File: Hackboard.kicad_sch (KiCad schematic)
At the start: 66 parts, among them J1 Conn_01x31_Socket, J2 Micro_SD_Card, J3 Conn_01x31_Socket, J5 Conn_02x02_Counter_Clockwise, J6 USB_C_Receptacle_USB2.0_16P, J7 Barrel_Jack_Switch, Q1 NMOS, Q2 NMOS, Q3 NMOS, SW1 SW_DPST, U1 NCP164CSN330T1G, U2 AP63205WU, U3 STM32L476RGT6, U4 74LVC4245APW, U5 74LVC4245APW, U6 74LVC4245APW, U7 USBLC6-2SC6, U8 74LVC4245APW, U9 74LVC4245APW

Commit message: Route power
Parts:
- added R16: 1M, symbol Device:R
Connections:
- net GND: now also R16.2; no longer J6.S1 (SHIELD)
- new net: J6.S1 (SHIELD), R16.1
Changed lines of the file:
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@@
 	)
 	(junction
+		(at 229.87 162.56)
+		(diameter 0)
+		(color 0 0 0 0)
+	)
+	(junction
 		(at 246.38 106.68)
 		(diameter 0)
@@
 	)
 	(junction
-		(at 229.87 162.56)
-		(diameter 0)
-		(color 0 0 0 0)
-	)
-	(junction
 		(at 62.23 19.05)
 		(diameter 0)
@@
 		)
 	)
-	(wire
-		(pts
-			(xy 222.25 162.56) (xy 229.87 162.56)
-		)
-		(stroke
-			(width 0)
-			(type default)
-		)
-	)
 	(polyline
 		(pts
@@
 					(unit 1)
 				)
+			)
+		)
+	)
+	(symbol
+		(lib_id "Device:R")
+		(at 226.06 162.56 90)
+		(unit 1)
+		(exclude_from_sim no)
+		(in_bom yes)
+		(on_board yes)
+		(dnp no)
+		(property "Reference" "R16"
+			(at 226.06 160.528 90)
+			(effects
+				(font
+					(size 1.27 1.27)
+				)
+			)
+		)
+		(property "Value" "1M"
+			(at 226.06 164.846 90)
+			(effects
+				(font
+					(size 1.27 1.27)
+				)
+			)
+		)
+		(property "Footprint" ""
+			(at 226.06 164.338 90)
+			(effects
+				(font
+					(size 1.27 1.27)
+				)
+				(hide yes)
+			)
+		)
+		(property "Datasheet" "~"
+			(at 226.06 162.56 0)
+			(effects
+				(font
+					(size 1.27 1.27)
+				)
+				(hide yes)
+			)
+		)
+		(property "Description" "Resistor"
+			(at 226.06 162.56 0)
+			(effects
+				(font
+					(size 1.27 1.27)
+				)
+				(hide yes)
+			)
+		)
+		(pin "2"
+		)
+		(pin "1"
+		)
+		(instances
+			(project "Hackboard"
+				(path "/478098fb-f4b2-4694-bef3-d53baad1e8cf"
+					(reference "R16")
+					(unit 1)
+				)

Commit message: Change USB C footprint, fix DRC errors, adjust silkscreen
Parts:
- J6: footprint Connector_USB:USB_C_Receptacle_GCT_USB4105-xx-A_16P_TopMnt_Horizontal -> Connector_USB:USB_C_Receptacle_Molex_216990
- R16: footprint (none) -> Resistor_SMD:R_0603_1608Metric
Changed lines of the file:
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@@
 			)
 		)
-		(property "Footprint" "Connector_USB:USB_C_Receptacle_GCT_USB4105-xx-A_16P_TopMnt_Horizontal"
+		(property "Footprint" "Connector_USB:USB_C_Receptacle_Molex_216990"
 			(at 233.68 139.7 0)
 			(effects
@@
 			)
 		)
-		(property "Footprint" ""
+		(property "Footprint" "Resistor_SMD:R_0603_1608Metric"
 			(at 226.06 164.338 90)
 			(effects

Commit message: Finish PCB
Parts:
- removed SW1: SW_DPST, Button_Switch_SMD:SW_SPST_PTS645, symbol Switch:SW_DPST_x2
- added R17, R18, R19, R20: 50k, Resistor_SMD:R_0603_1608Metric, symbol Device:R
- added SW1: SW_SPST, Button_Switch_SMD:SW_SPST_PTS645, symbol Switch:SW_SPST
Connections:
- net +3V3: now also R17.1, R18.1, R19.1, R20.1
- net GND: now also SW1.1 (A)
- net PWM_PIN2: now also U6.14 (B5); no longer JP2.1 (A)
- net PWM_PIN2_O: now also JP2.2 (B); no longer U6.8 (A5)
- net RESET: now also SW1.2 (B)
- net SD_CS_PWM_26: now also R20.2
- net SD_MISO_PWM_28: now also R17.2
- net SD_MOSI_GPIO_PIN4: now also R19.2
- net SD_SCK_DAC_A8: now also R18.2
- new net: JP2.1 (A), U6.8 (A5)
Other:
- moved on the sheet: J2, J5, Q2, Q3, R10, R11, R14, R15, U4, U5, U6, U8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

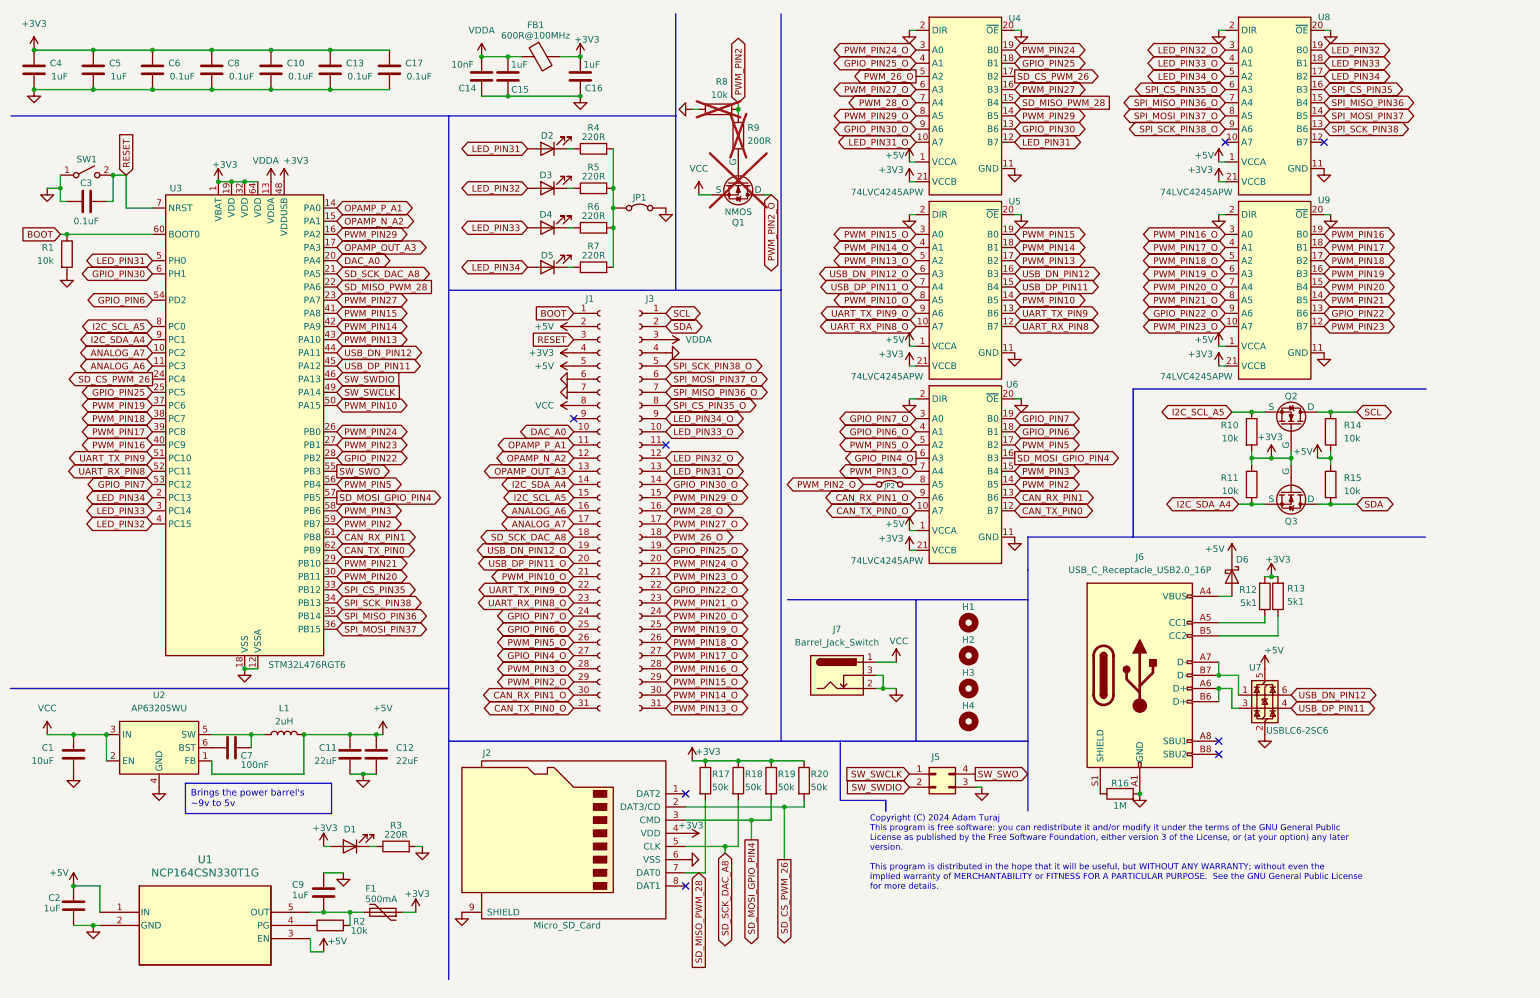
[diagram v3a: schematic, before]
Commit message: Change MCU Pinout
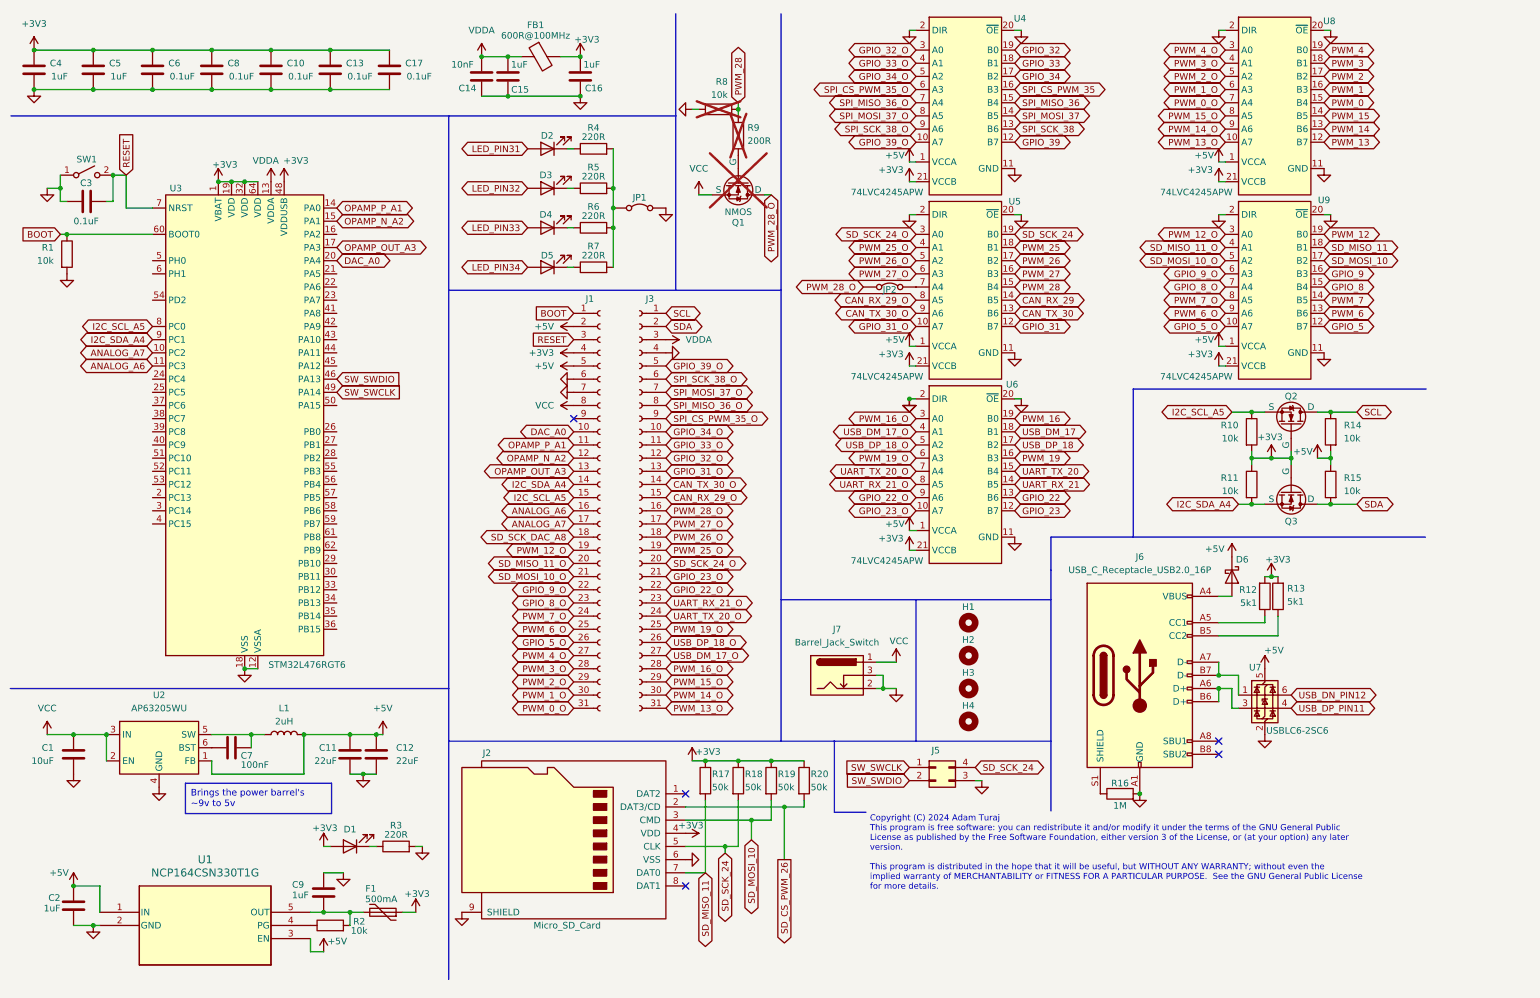
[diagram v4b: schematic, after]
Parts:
- JP2: footprint Jumper:SolderJumper-2_P1.3mm_Open_RoundedPad1.0x1.5mm -> (none)
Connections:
- net LED_PIN31: no longer U3.5 (PH0), U4.12 (B7)
- net LED_PIN32: no longer U3.4 (PC15), U8.19 (B0)
- net LED_PIN33: no longer U3.3 (PC14), U8.18 (B1)
- net LED_PIN34: no longer U3.2 (PC13), U8.17 (B2)
- net PWM_26_O: now also U5.5 (A2); no longer U4.5 (A2)
- net PWM_28_O: now also JP2.1 (A), Q1.1 (D); no longer U4.7 (A4)
- net SD_CS_PWM_26: no longer U3.24 (PC4), U4.17 (B2)
- net SD_SCK_DAC_A8: no longer J2.5 (CLK), R18.2, U3.21 (PA5)
- net USB_DN_PIN12: no longer U3.44 (PA11), U5.16 (B3)
- net USB_DP_PIN11: no longer U3.45 (PA12), U5.15 (B4)
- net PWM_13_O: now reaches U8.10 (A7)
- net PWM_13_O: now also J3.31 (Pin_31)
- net PWM_13: now reaches U8.12 (B7)
- net UART_RX_21_O: now reaches U6.8 (A5)
- net UART_RX_21_O: now also J3.23 (Pin_23); no longer JP2.1 (A)
- net GPIO_33_O: now reaches J3.11 (Pin_11)
- net GPIO_33_O: now also U4.4 (A1)
- net CAN_RX_PIN1: no longer names the net of U3.61 (PB8)
- net CAN_RX_PIN1: no longer U6.13 (B6)
- net CAN_RX_PIN1_O renamed GPIO_22_O
- net GPIO_22_O: now also J3.22 (Pin_22); no longer J1.30 (Pin_30)
- net CAN_TX_PIN0: no longer names the net of U3.62 (PB9)
- net CAN_TX_PIN0: no longer U6.12 (B7)
- net CAN_TX_PIN0_O renamed GPIO_23_O
- net GPIO_23_O: now also J3.21 (Pin_21); no longer J1.31 (Pin_31)
- net GPIO_PIN22: no longer names the net of U3.28 (PB2)
- net GPIO_PIN22: no longer U9.13 (B6)
- net GPIO_PIN22_O renamed PWM_6_O
- net PWM_6_O: now also J1.25 (Pin_25); no longer J3.22 (Pin_22)
- net GPIO_PIN25: no longer names the net of U3.25 (PC5)
- net GPIO_PIN25: no longer U4.18 (B1)
- net GPIO_PIN25_O renamed PWM_25_O
- net PWM_25_O: now also U5.4 (A1); no longer U4.4 (A1)
- net GPIO_PIN30: no longer names the net of U3.6 (PH1)
- net GPIO_PIN30: no longer U4.13 (B6)
- net GPIO_PIN30_O renamed CAN_TX_30_O
- net CAN_TX_30_O: now also U5.9 (A6); no longer U4.9 (A6)
- net GPIO_PIN4_O renamed PWM_19_O
- net PWM_19_O: now also J3.25 (Pin_25); no longer J1.27 (Pin_27)
- net GPIO_PIN6: no longer names the net of U3.54 (PD2)
- net GPIO_PIN6: no longer U6.18 (B1)
- net GPIO_PIN6_O renamed USB_DM_17_O
- net USB_DM_17_O: now also J3.27 (Pin_27); no longer J1.25 (Pin_25)
- net GPIO_PIN7: no longer names the net of U3.53 (PC12)
- net GPIO_PIN7: no longer U6.19 (B0)
- net GPIO_PIN7_O renamed PWM_16_O
- net PWM_16_O: now also J3.28 (Pin_28); no longer J1.24 (Pin_24)
- net LED_PIN31_O renamed GPIO_31_O
- net GPIO_31_O: now also U5.10 (A7); no longer U4.10 (A7)
- net LED_PIN32_O renamed GPIO_32_O
- net GPIO_32_O: now also U4.3 (A0); no longer U8.3 (A0)
- net LED_PIN33_O renamed GPIO_34_O
- net GPIO_34_O: now also U4.5 (A2); no longer U8.4 (A1)
- net LED_PIN34_O renamed PWM_2_O
- net PWM_2_O: now also J1.29 (Pin_29); no longer J3.9 (Pin_9)
- net PWM_PIN10: no longer names the net of U3.50 (PA15)
- net PWM_PIN10: no longer U5.14 (B5)
- net PWM_PIN10_O renamed CAN_RX_29_O
- net CAN_RX_29_O: now also J3.15 (Pin_15); no longer J1.21 (Pin_21)
- net PWM_PIN13: no longer names the net of U3.43 (PA10)
- net PWM_PIN13: no longer U5.17 (B2)
- removed net PWM_PIN13_O: J3.31 (Pin_31), U5.5 (A2)
- net PWM_PIN14: no longer names the net of U3.42 (PA9)
- net PWM_PIN14: no longer U5.18 (B1)
- net PWM_PIN14_O renamed PWM_14_O
- net PWM_14_O: now also U8.9 (A6); no longer U5.4 (A1)
- net PWM_PIN15: no longer names the net of U3.41 (PA8)
- net PWM_PIN15: no longer U5.19 (B0)
- net PWM_PIN15_O renamed PWM_15_O
- net PWM_15_O: now also U8.8 (A5); no longer U5.3 (A0)
- net PWM_PIN16: no longer names the net of U3.40 (PC9)
- net PWM_PIN16: no longer U9.19 (B0)
- net PWM_PIN16_O renamed PWM_12_O
- net PWM_12_O: now also J1.19 (Pin_19); no longer J3.28 (Pin_28)
- net PWM_PIN17: no longer names the net of U3.39 (PC8)
- net PWM_PIN17: no longer U9.18 (B1)
- net PWM_PIN17_O renamed SD_MISO_11_O
- net SD_MISO_11_O: now also J1.20 (Pin_20); no longer J3.27 (Pin_27)
- net PWM_PIN18: no longer names the net of U3.38 (PC7)
- net PWM_PIN18: no longer U9.17 (B2)
- net PWM_PIN18_O renamed SD_MOSI_10_O
- net SD_MOSI_10_O: now also J1.21 (Pin_21); no longer J3.26 (Pin_26)
- net PWM_PIN19: no longer names the net of U3.37 (PC6)
- net PWM_PIN19: no longer U9.16 (B3)
- net PWM_PIN19_O renamed GPIO_9_O
- net GPIO_9_O: now also J1.22 (Pin_22); no longer J3.25 (Pin_25)
- net PWM_PIN2 renamed PWM_28
- net PWM_28: now also U5.15 (B4); no longer U3.59 (PB7), U6.14 (B5)
- net PWM_PIN20: no longer names the net of U3.30 (PB11)
- net PWM_PIN20: no longer U9.15 (B4)
- net PWM_PIN20_O renamed GPIO_8_O
- net GPIO_8_O: now also J1.23 (Pin_23); no longer J3.24 (Pin_24)
- net PWM_PIN21: no longer names the net of U3.29 (PB10)
- net PWM_PIN21: no longer U9.14 (B5)
- net PWM_PIN21_O renamed PWM_7_O
- net PWM_7_O: now also J1.24 (Pin_24); no longer J3.23 (Pin_23)
- net PWM_PIN23: no longer names the net of U3.27 (PB1)
- net PWM_PIN23: no longer U9.12 (B7)
- net PWM_PIN23_O renamed GPIO_5_O
- net GPIO_5_O: now also J1.26 (Pin_26); no longer J3.21 (Pin_21)
- net PWM_PIN24: no longer names the net of U3.26 (PB0)
- net PWM_PIN24: no longer U4.19 (B0)
- net PWM_PIN24_O renamed SD_SCK_24_O
- net SD_SCK_24_O: now also U5.3 (A0); no longer U4.3 (A0)
- net PWM_PIN27: no longer names the net of U3.23 (PA7)
- net PWM_PIN27: no longer U4.16 (B3)
- net PWM_PIN27_O renamed PWM_27_O
- net PWM_27_O: now also U5.6 (A3); no longer U4.6 (A3)
- net PWM_PIN29: no longer names the net of U3.16 (PA2)
- net PWM_PIN29: no longer U4.14 (B5)
- net PWM_PIN29_O renamed SPI_MOSI_37_O
- net SPI_MOSI_37_O: now also J3.7 (Pin_7); no longer J3.15 (Pin_15)
- removed net PWM_PIN2_O: J1.29 (Pin_29), JP2.2 (B), Q1.1 (D)
- net PWM_PIN3: no longer names the net of U3.58 (PB6)
- net PWM_PIN3: no longer U6.15 (B4)
- net PWM_PIN3_O renamed PWM_3_O
- net PWM_3_O: now also U8.4 (A1); no longer U6.7 (A4)
- net PWM_PIN5: no longer names the net of U3.56 (PB4)
- net PWM_PIN5: no longer U6.17 (B2)
- net PWM_PIN5_O renamed USB_DP_18_O
- net USB_DP_18_O: now also J3.26 (Pin_26); no longer J1.26 (Pin_26)
- net SD_MISO_PWM_28 renamed SD_MISO_11
- net SD_MISO_11: now also U9.18 (B1); no longer U3.22 (PA6), U4.15 (B4)
- net SD_MOSI_GPIO_PIN4 renamed SD_MOSI_10
- net SD_MOSI_10: now also U9.17 (B2); no longer U3.57 (PB5), U6.16 (B3)
- net SPI_CS_PIN35: no longer names the net of U3.33 (PB12)
- net SPI_CS_PIN35: no longer U8.16 (B3)
- net SPI_CS_PIN35_O renamed PWM_1_O
- net PWM_1_O: now also J1.30 (Pin_30); no longer J3.8 (Pin_8)
- net SPI_MISO_PIN36: no longer names the net of U3.35 (PB14)
- net SPI_MISO_PIN36: no longer U8.15 (B4)
- net SPI_MISO_PIN36_O renamed PWM_0_O
- net PWM_0_O: now also J1.31 (Pin_31); no longer J3.7 (Pin_7)
- net SPI_MOSI_PIN37: no longer names the net of U3.36 (PB15)
- net SPI_MOSI_PIN37: no longer U8.14 (B5)
- net SPI_MOSI_PIN37_O renamed SPI_SCK_38_O
- net SPI_SCK_38_O: now also U4.9 (A6); no longer U8.8 (A5)
- net SPI_SCK_PIN38: no longer names the net of U3.34 (PB13)
- net SPI_SCK_PIN38: no longer U8.13 (B6)
- net SPI_SCK_PIN38_O renamed GPIO_39_O
- net GPIO_39_O: now also U4.10 (A7); no longer U8.9 (A6)
- net SW_SWO: no longer names the net of U3.55 (PB3)
- net SW_SWO: no longer J5.4 (Pin_4)
- net UART_RX_PIN8: no longer names the net of U3.52 (PC11)
- net UART_RX_PIN8: no longer U5.12 (B7)
- removed net UART_RX_PIN8_O: J1.23 (Pin_23), U5.10 (A7)
- net UART_TX_PIN9: no longer names the net of U3.51 (PC10)
- net UART_TX_PIN9: no longer U5.13 (B6)
- removed net UART_TX_PIN9_O: J1.22 (Pin_22), U5.9 (A6)
- removed net USB_DN_PIN12_O: J1.19 (Pin_19), U5.6 (A3)
- net USB_DP_PIN11_O: no longer names the net of U5.7 (A4)
- net USB_DP_PIN11_O: now also JP2.2 (B); no longer J1.20 (Pin_20)
- new net CAN_RX_29: U5.14 (B5)
- new net CAN_TX_30: U5.13 (B6)
- new net GPIO_22: U6.13 (B6)
- new net GPIO_23: U6.12 (B7)
- new net GPIO_31: U5.12 (B7)
- new net GPIO_32: U4.19 (B0)
- new net GPIO_33: U4.18 (B1)
- new net GPIO_34: U4.17 (B2)
- new net GPIO_39: U4.12 (B7)
- new net GPIO_5: U9.12 (B7)
- new net GPIO_8: U9.15 (B4)
- new net GPIO_9: U9.16 (B3)
- new net PWM_0: U8.15 (B4)
- new net PWM_1: U8.16 (B3)
- new net PWM_12: U9.19 (B0)
- new net PWM_14: U8.13 (B6)
- new net PWM_15: U8.14 (B5)
- new net PWM_16: U6.19 (B0)
- new net PWM_19: U6.16 (B3)
- new net PWM_2: U8.17 (B2)
- new net PWM_25: U5.18 (B1)
- new net PWM_26: U5.17 (B2)
- new net PWM_27: U5.16 (B3)
- new net PWM_3: U8.18 (B1)
- new net PWM_4: U8.19 (B0)
- new net PWM_4_O: J1.27 (Pin_27), U8.3 (A0)
- new net PWM_6: U9.13 (B6)
- new net PWM_7: U9.14 (B5)
- new net SD_SCK_24: J2.5 (CLK), J5.4 (Pin_4), R18.2, U5.19 (B0)
- new net SPI_CS_PWM_35: U4.16 (B3)
- new net SPI_CS_PWM_35_O: J3.9 (Pin_9), U4.6 (A3)
- new net SPI_MISO_36: U4.15 (B4)
- new net SPI_MISO_36_O: J3.8 (Pin_8), U4.7 (A4)
- new net SPI_MOSI_37: U4.14 (B5)
- new net SPI_SCK_38: U4.13 (B6)
- new net UART_RX_21: U6.14 (B5)
- new net UART_TX_20: U6.15 (B4)
- new net UART_TX_20_O: J3.24 (Pin_24), U6.7 (A4)
- new net USB_DM_17: U6.18 (B1)
- new net USB_DP_18: U6.17 (B2)
- no-connect marks 8 -> 5
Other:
- moved on the sheet: J5

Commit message: Finish up updated schematic, start outlining border
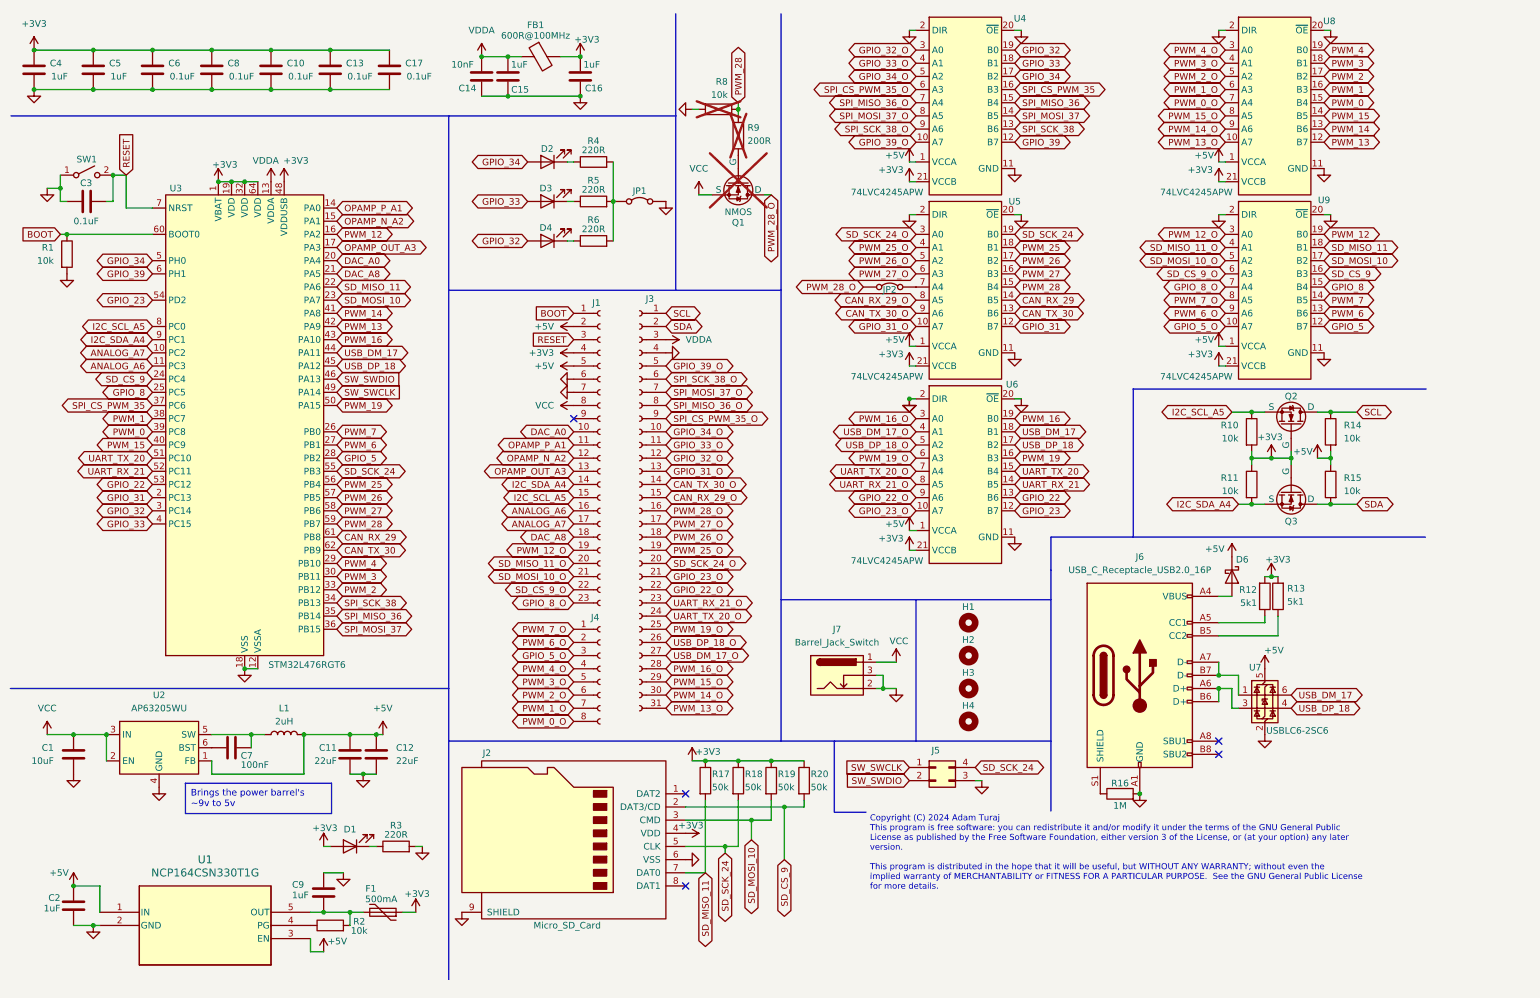
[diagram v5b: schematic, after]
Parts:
- removed D5: LED, LED_SMD:LED_0603_1608Metric, symbol Device:LED
- removed J1: Conn_01x31_Socket, Connector_PinHeader_2.54mm:PinHeader_1x31_P2.54mm_Vertical, symbol Connector:Conn_01x31_Socket
- removed R7: 220R, Resistor_SMD:R_0603_1608Metric, symbol Device:R
- added J1: Conn_01x23_Socket, Connector_PinHeader_2.54mm:PinHeader_1x23_P2.54mm_Vertical, symbol Connector:Conn_01x23_Socket
- added J4: Conn_01x08_Socket, Connector_PinHeader_2.54mm:PinHeader_1x08_P2.54mm_Vertical, symbol Connector:Conn_01x08_Socket
- JP2: footprint (none) -> Jumper:SolderJumper-2_P1.3mm_Open_RoundedPad1.0x1.5mm
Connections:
- net GPIO_9 is gone; now on net SD_CS_9: U9.16 (B3)
- net LED_PIN31 is gone; now on net GPIO_34: D2.2 (A)
- net LED_PIN32 is gone; now on net GPIO_33: D3.2 (A)
- net LED_PIN33 is gone; now on net GPIO_32: D4.2 (A)
- net SD_CS_PWM_26 is gone; now on net SD_CS_9: J2.2 (DAT3/CD), R20.2
- net USB_DN_PIN12 is gone; now on net USB_DM_17: U7.6 (I/O1)
- net USB_DP_PIN11 is gone; now on net USB_DP_18: U7.4 (I/O2)
- net +3V3: now also J1.4 (Pin_4)
- net +5V: now also J1.2 (Pin_2), J1.5 (Pin_5)
- net ANALOG_A6: now also J1.16 (Pin_16)
- net ANALOG_A7: now also J1.17 (Pin_17)
- net BOOT: now also J1.1 (Pin_1)
- net CAN_RX_29: now also U3.61 (PB8)
- net CAN_TX_30: now also U3.62 (PB9)
- net DAC_A0: now also J1.10 (Pin_10)
- net GND: now also J1.6 (Pin_6), J1.7 (Pin_7)
- net GPIO_22: now also U3.53 (PC12)
- net GPIO_23: now also U3.54 (PD2)
- net GPIO_31: now also U3.2 (PC13)
- net GPIO_32: now also U3.3 (PC14)
- net GPIO_33: now also U3.4 (PC15)
- net GPIO_34: now also U3.5 (PH0)
- net GPIO_39: now also U3.6 (PH1)
- net GPIO_5: now also U3.28 (PB2)
- net GPIO_5_O: now also J4.3 (Pin_3)
- net GPIO_8: now also U3.25 (PC5)
- net GPIO_8_O: now also J1.23 (Pin_23)
- net I2C_SCL_A5: now also J1.15 (Pin_15)
- net I2C_SDA_A4: now also J1.14 (Pin_14)
- net OPAMP_N_A2: now also J1.12 (Pin_12)
- net OPAMP_OUT_A3: now also J1.13 (Pin_13)
- net OPAMP_P_A1: now also J1.11 (Pin_11)
- net PWM_0: now also U3.39 (PC8)
- net PWM_0_O: now also J4.8 (Pin_8)
- net PWM_1: now also U3.38 (PC7)
- net PWM_12: now also U3.16 (PA2)
- net PWM_12_O: now also J1.19 (Pin_19)
- net PWM_13: now also U3.42 (PA9)
- net PWM_14: now also U3.41 (PA8)
- net PWM_15: now also U3.40 (PC9)
- net PWM_16: now also U3.43 (PA10)
- net PWM_19: now also U3.50 (PA15)
- net PWM_1_O: now also J4.7 (Pin_7)
- net PWM_2: now also U3.33 (PB12)
- net PWM_25: now also U3.56 (PB4)
- net PWM_26: now also U3.57 (PB5)
- net PWM_27: now also U3.58 (PB6)
- net PWM_28: now also U3.59 (PB7)
- net PWM_2_O: now also J4.6 (Pin_6)
- net PWM_3: now also U3.30 (PB11)
- net PWM_3_O: now also J4.5 (Pin_5)
- net PWM_4: now also U3.29 (PB10)
- net PWM_4_O: now also J4.4 (Pin_4)
- net PWM_6: now also U3.27 (PB1)
- net PWM_6_O: now also J4.2 (Pin_2)
- net PWM_7: now also U3.26 (PB0)
- net PWM_7_O: now also J4.1 (Pin_1)
- net RESET: now also J1.3 (Pin_3)
- net SD_MISO_11: now also U3.22 (PA6)
- net SD_MISO_11_O: now also J1.20 (Pin_20)
- net SD_MOSI_10: now also U3.23 (PA7)
- net SD_MOSI_10_O: now also J1.21 (Pin_21)
- net SD_SCK_24: now also U3.55 (PB3)
- net SPI_CS_PWM_35: now also U3.37 (PC6)
- net SPI_MISO_36: now also U3.35 (PB14)
- net SPI_MOSI_37: now also U3.36 (PB15)
- net SPI_SCK_38: now also U3.34 (PB13)
- net UART_RX_21: now also U3.52 (PC11)
- net UART_TX_20: now also U3.51 (PC10)
- net USB_DM_17: now also U3.44 (PA11)
- net USB_DP_18: now also U3.45 (PA12)
- net VCC: now also J1.8 (Pin_8)
- net DAC_A8: now reaches U3.21 (PA5)
- net DAC_A8: now also J1.18 (Pin_18)
- net SD_CS_9: now reaches U3.24 (PC4)
- net GPIO_9_O renamed SD_CS_9_O
- net SD_CS_9_O: now also J1.22 (Pin_22)
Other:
- moved on the sheet: D2, D3, D4, JP1, R4, R5, R6
